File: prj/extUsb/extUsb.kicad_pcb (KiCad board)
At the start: 2 copper layers, 21.6 x 14.2 mm, 6 parts, among them J1 USB_B_Micro, J2 Conn_01x05, U1 SN74LVC2T45

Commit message: extUsb Redo after attempt2 experiments and add 3.3V rail.
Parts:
- added C1: 18p, Capacitor_SMD:C_0603_1608Metric_Pad1.08x0.95mm_HandSolder, F.Cu at (-509.3, -208.5)
- added C2: 18p, Capacitor_SMD:C_0603_1608Metric_Pad1.08x0.95mm_HandSolder, F.Cu at (-506.7, -214.9)
- added C3: 100n, Capacitor_SMD:C_0603_1608Metric_Pad1.08x0.95mm_HandSolder, F.Cu at (-499.1, -207.8)
- added C4: 100n, Capacitor_SMD:C_0603_1608Metric_Pad1.08x0.95mm_HandSolder, F.Cu at (-499.1, -214.9)
- added C5: 10u, Capacitor_SMD:C_0603_1608Metric_Pad1.08x0.95mm_HandSolder, F.Cu at (-509.5, -216.2)
- added FB1: Ferrite_Bead, Inductor_SMD:L_0603_1608Metric_Pad1.05x0.95mm_HandSolder, F.Cu at (-512.3, -217.2)
- added Q1: Q_NMOS_GSD, Package_TO_SOT_SMD:SOT-23_Handsoldering, F.Cu at (-503.7, -208.5)
- added R4: 10k, Resistor_SMD:R_0603_1608Metric_Pad0.98x0.95mm_HandSolder, F.Cu at (-499.1, -209.6)
- added U2: MIC5504-3.3YM5, Package_TO_SOT_SMD:SOT-23-5, F.Cu at (-502.9, -215.9)
- J2: moved to B.Cu
- R1: value 1k5 -> 33
- R2: value 68 -> 33
- R3: value 68 -> 1k5
- moved R1 735.0 mm to (-506.7, -211.3)
- moved J1 734.9 mm to (-513.1, -211.8)
- moved R2 734.7 mm to (-506.7, -213.1)
- moved R3 733.0 mm to (-507.5, -208.5), turned to 90 degrees
- moved U1 732.8 mm to (-500.6, -212.1), turned to 180 degrees
- moved J2 729.8 mm to (-495.8, -206.8)
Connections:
- J1 pad 1: Vusb -> Net-(FB1-Pad2)
- J2 pad 2: pin_usb_oe -> Vext
- J2 pad 3: Vext -> pin_usb_p
- J2 pad 4: pin_usb_p -> pin_usb_n
- J2 pad 5: pin_usb_n -> pin_usb_oe
- R1 pad 1: Vusb -> Net-(R1-Pad1)
- R2 pad 2: usb_p -> usb_n
- R3 pad 1: Net-(R3-Pad1) -> Net-(Q1-Pad2)
- R3 pad 2: usb_n -> usb_p
- U1 pad 6: Net-(R3-Pad1) -> Net-(R2-Pad1)
- U1 pad 7: Net-(R2-Pad1) -> Net-(R1-Pad1)
- U1 pad 8: Vusb -> +3V3
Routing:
- net GND: track 43.7 -> 74.9 mm
- net Vusb: track 18.6 -> 0.00 mm
- net +5V: track 0.00 -> 11.2 mm
- net +3V3: track 0.00 -> 11.2 mm
- net Vext: track 8.08 -> 14.5 mm
- net Net-(R3-Pad1): track 5.31 -> 0.00 mm
- net pin_usb_oe: track 4.75 -> 10.0 mm
- net pin_usb_n: track 9.17 -> 3.94 mm
- net Net-(FB1-Pad2): track 0.00 -> 5.23 mm
- net pin_usb_p: track 8.12 -> 3.16 mm
- net Net-(R1-Pad1): track 0.00 -> 3.66 mm
- net Net-(Q1-Pad2): track 0.00 -> 2.33 mm
- net usb_p: track 5.81 -> 7.93 mm
- net usb_n: track 4.03 -> 6.03 mm
- net Net-(R2-Pad1): track 5.75 -> 3.77 mm
- removed copper zone on B.Cu, net GND
- removed copper zone on F.Cu, net GND
- removed copper zone on B.Cu, net Vext
- removed copper zone on F.Cu, net Vext
- removed copper zone on F.Cu, net Vusb
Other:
- board outline removed
- rule pad_to_mask_clearance: 0 -> 0.05
- board text removed: "GND"
- board text removed: "Vext"
- board text removed: "ext D+"
- board text removed: "ext D-"
- board text removed: "ext oe"
- board text removed: "extUsb"

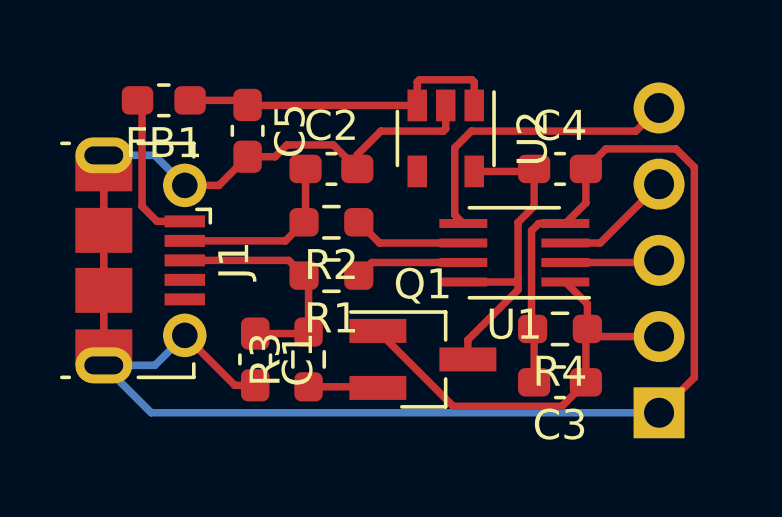
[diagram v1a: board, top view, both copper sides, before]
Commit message: extUsb Layout for hand-solder
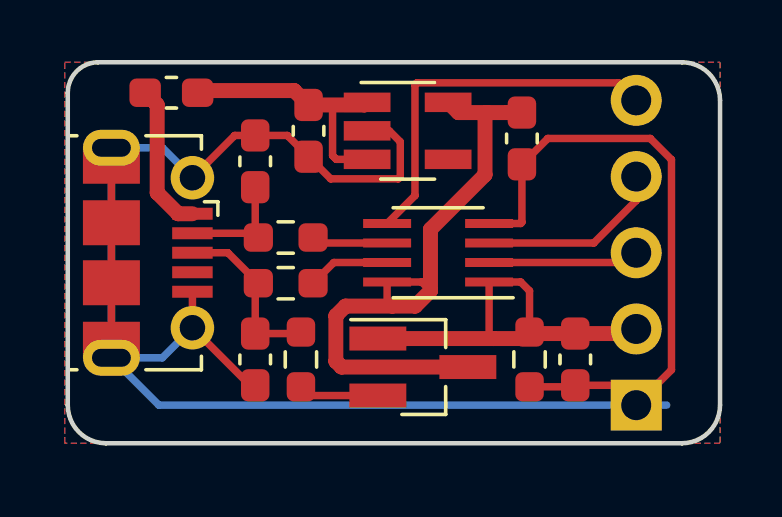
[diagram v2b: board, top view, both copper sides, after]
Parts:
- U2: footprint Package_TO_SOT_SMD:SOT-23-5 -> Package_TO_SOT_SMD:SOT-23-5_HandSoldering
- moved C2 2.55 mm to (-509.3, -215.1), turned to 90 degrees
- moved U1 2.54 mm to (-503.2, -212.1)
- moved C5 2.03 mm to (-507.5, -216.2)
- moved C4 1.63 mm to (-500.4, -215.9), turned to 270 degrees
- moved R2 1.61 mm to (-508.3, -212.6)
- moved R1 1.55 mm to (-508.3, -211.1)
- moved R4 1.44 mm to (-500.1, -208.5), turned to 270 degrees
- moved U2 1.30 mm to (-504.2, -216.2), turned to 0 degrees
- moved C3 0.92 mm to (-498.6, -208.5), turned to 270 degrees
- moved J2 0.80 mm to (-496.6, -207.0)
- moved FB1 0.36 mm to (-512.1, -217.4)
- moved J1 0.36 mm to (-512.8, -212.1)
- moved Q1 0.25 mm to (-503.7, -208.3)
- moved R3 0.25 mm to (-507.7, -208.5)
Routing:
- net +3V3: track 11.2 -> 21.7 mm
- net pin_usb_oe: track 10.0 -> 12.7 mm
- net pin_usb_n: track 3.94 -> 6.29 mm
- net usb_n: track 6.03 -> 3.83 mm
- net usb_p: track 7.93 -> 5.88 mm
- net pin_usb_p: track 3.16 -> 5.04 mm
- net Net-(R2-Pad1): track 3.77 -> 2.54 mm
- net Net-(R1-Pad1): track 3.66 -> 2.75 mm
- net +5V: track 11.2 -> 10.3 mm
- net Vext: track 14.5 -> 13.6 mm
- added copper zone on B.Cu, net GND
- added copper zone on F.Cu, net GND
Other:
- board outline added: 21.7 x 12.7 mm
- board text added: "D+"
- board text added: "D-"
- board text added: "GND"
- board text added: "Vext"
- board text added: "extUsb USB-FS levelshifter"
- board text added: "oe"

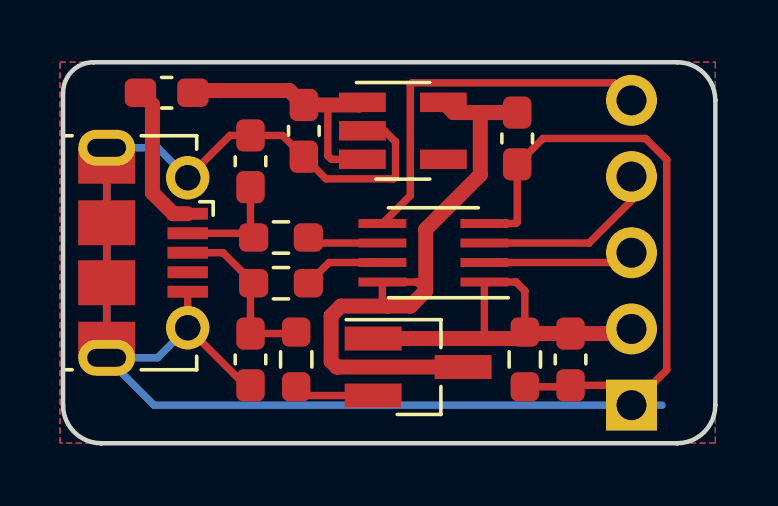
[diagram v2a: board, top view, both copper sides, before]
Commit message: extUsb Higher priority zones for 3.3V and 5V, and gerber plot settings.
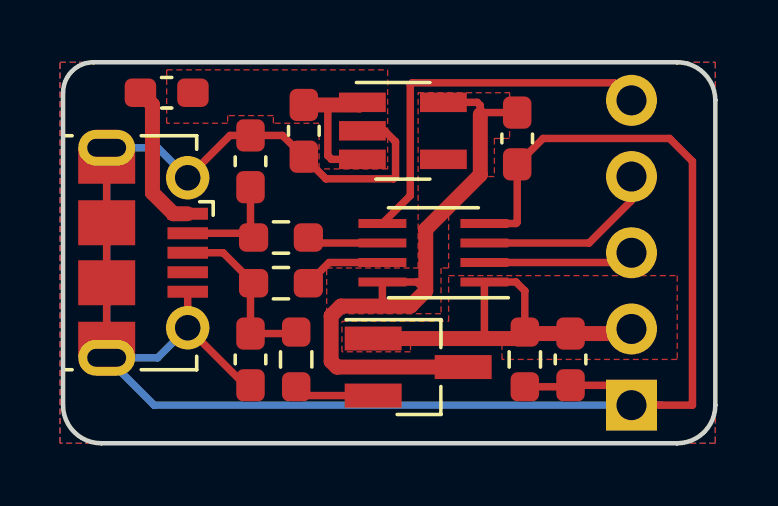
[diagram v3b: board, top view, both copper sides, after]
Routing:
- net +5V: track 10.3 -> 6.25 mm
- net GND: track 75.0 -> 77.4 mm
- added copper zone on F.Cu, net +3V3
- added copper zone on F.Cu, net +5V
- added copper zone on F.Cu, net Vext
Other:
- rule pad_to_mask_clearance: 0.05 -> 0

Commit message: extUsb Analog switch for 1k5 pullup
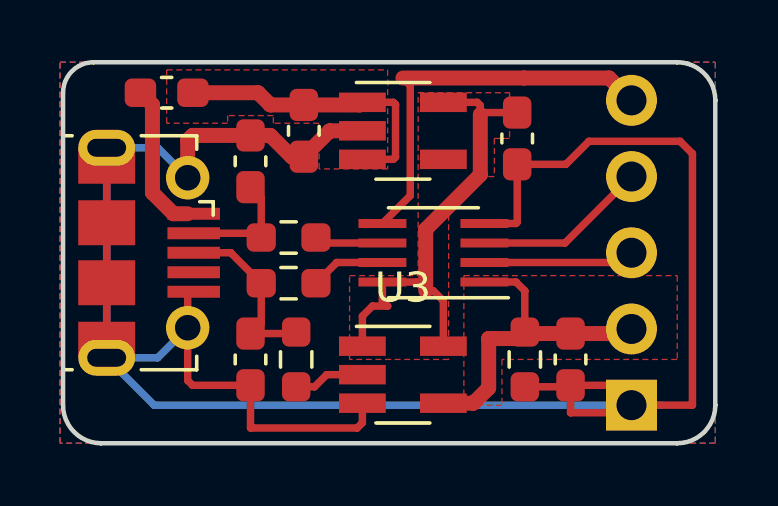
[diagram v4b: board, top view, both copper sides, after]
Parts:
- removed Q1: Q_NMOS_GSD, Package_TO_SOT_SMD:SOT-23_Handsoldering
- added U3: TS5A3166DBVR, Package_TO_SOT_SMD:SOT-23-5_HandSoldering, F.Cu at (-504.2, -208.0)
- moved R1 0.25 mm to (-508.0, -211.1)
- moved R2 0.25 mm to (-508.0, -212.6)
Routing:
- net GND: track 77.4 -> 84.8 mm
- net +3V3: track 21.4 -> 16.1 mm
- net +5V: track 6.25 -> 11.0 mm
- net Vext: track 13.6 -> 11.1 mm
- net pin_usb_oe: track 12.7 -> 13.3 mm
- net usb_n: track 3.83 -> 4.34 mm
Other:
- rule trace_min: 0.2 -> 0.25

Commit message: extUsb Testpoints and many minor improvements to layout.
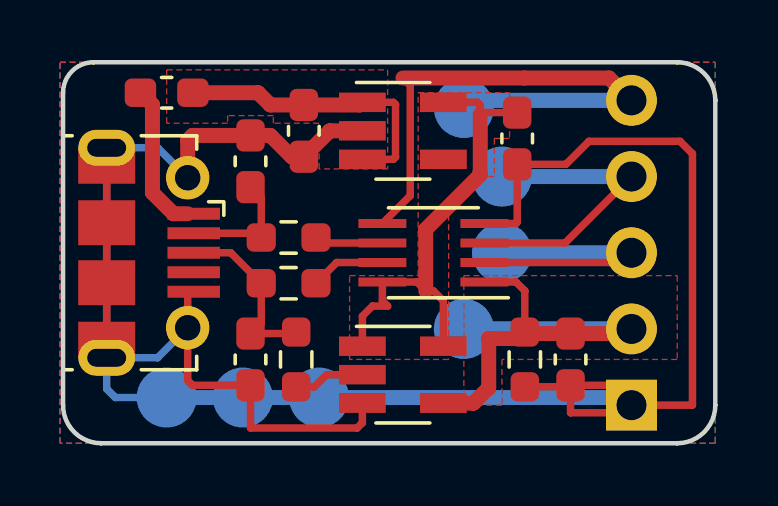
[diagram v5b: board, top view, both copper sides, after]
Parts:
- added REF**: TestPoint_DemaskFillzone, extUsb:TestPoint_DemaskFillzone, F.Cu at (-509.3, -217.4)
- added REF**: TestPoint_DemaskFillzone, extUsb:TestPoint_DemaskFillzone, F.Cu at (-502.7, -214.1)
- added TP1: TestPoint, extUsb:TestPoint_Pad_D2.0mm, B.Cu at (-500.9, -212.1)
- added TP2: TestPoint, extUsb:TestPoint_Pad_D2.0mm, B.Cu at (-500.9, -214.6)
- added TP3: TestPoint, extUsb:TestPoint_Pad_D2.0mm, B.Cu at (-502.2, -216.9)
- added TP4: TestPoint, extUsb:TestPoint_Pad_D2.0mm, B.Cu at (-507.0, -207.3)
- added TP5: TestPoint, extUsb:TestPoint_Pad_D2.0mm, B.Cu at (-509.5, -207.3)
- added TP6: TestPoint, extUsb:TestPoint_Pad_D2.0mm, B.Cu at (-512.1, -207.3)
- added TP7: TestPoint, extUsb:TestPoint_Pad_D2.0mm, B.Cu at (-502.2, -209.6)
- C1, C2, C3, C4, C5: footprint Capacitor_SMD:C_0603_1608Metric_Pad1.08x0.95mm_HandSolder -> extUsb:C_0603_1608Metric_Pad1.08x0.95mm_HandSolder
- FB1: footprint Inductor_SMD:L_0603_1608Metric_Pad1.05x0.95mm_HandSolder -> extUsb:L_0603_1608Metric_Pad1.05x0.95mm_HandSolder
- J1: footprint Connector_USB:USB_Micro-B_Molex-105017-0001 -> extUsb:USB_Micro-B_Molex-105017-0001
- J2: footprint Connector_PinHeader_2.54mm:PinHeader_1x05_P2.54mm_Horizontal -> extUsb:PinHeader_1x05_P2.54mm_Horizontal
- R1, R2, R3, R4: footprint Resistor_SMD:R_0603_1608Metric_Pad0.98x0.95mm_HandSolder -> extUsb:R_0603_1608Metric_Pad0.98x0.95mm_HandSolder
- U1: footprint Package_SO:SSOP-8_2.95x2.8mm_P0.65mm -> extUsb:SSOP-8_2.95x2.8mm_P0.65mm
- U2, U3: footprint Package_TO_SOT_SMD:SOT-23-5_HandSoldering -> extUsb:SOT-23-5_HandSoldering
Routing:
- net pin_usb_oe: track 13.3 -> 19.0 mm
- net Vext: track 11.1 -> 16.7 mm
- net pin_usb_n: track 5.82 -> 10.1 mm
- net pin_usb_p: track 5.04 -> 9.36 mm

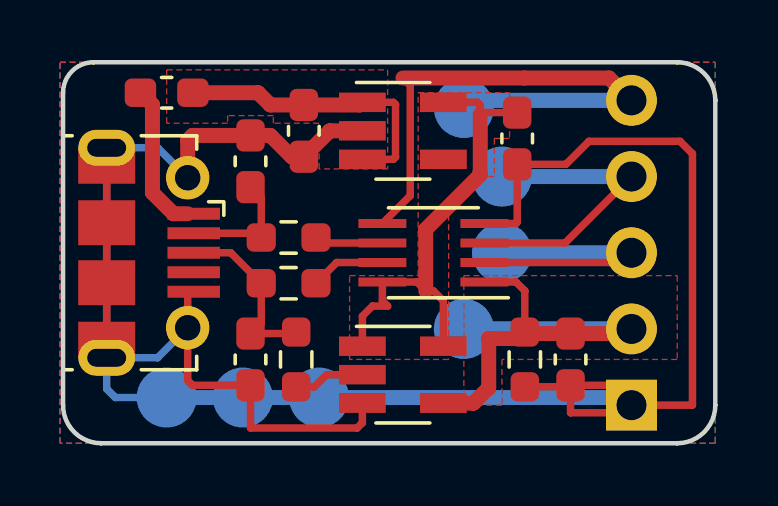
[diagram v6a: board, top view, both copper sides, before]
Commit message: extUsb version3 without short on body of USB connector.
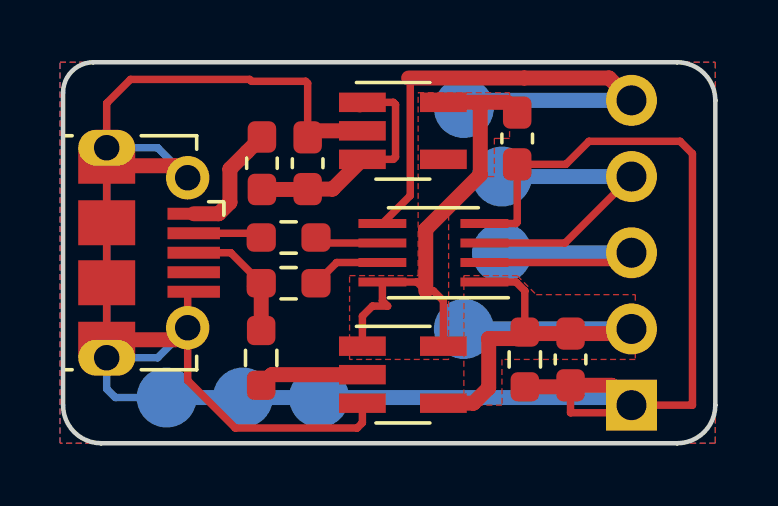
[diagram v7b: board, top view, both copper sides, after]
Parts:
- removed C1, C2: 18p, extUsb:C_0603_1608Metric_Pad1.08x0.95mm_HandSolder
- removed REF** (x2): TestPoint_DemaskFillzone, extUsb:TestPoint_DemaskFillzone
- moved FB1 3.95 mm to (-508.9, -215.1), turned to 90 degrees
- moved R3 1.17 mm to (-508.9, -208.6)
- moved C5 1.09 mm to (-507.4, -215.1), turned to 90 degrees
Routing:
- net GND: track 84.4 -> 94.2 mm
- net +5V: track 11.0 -> 7.91 mm
- net usb_n: track 4.34 -> 2.51 mm
- net usb_p: track 6.33 -> 5.00 mm
- net Net-(R3-Pad1): track 2.37 -> 3.52 mm
- net +3V3: track 16.1 -> 16.9 mm
- net pin_usb_oe: track 19.0 -> 18.4 mm
- net Net-(FB1-Pad2): track 5.18 -> 4.66 mm
- removed copper zone on F.Cu, net +5V
